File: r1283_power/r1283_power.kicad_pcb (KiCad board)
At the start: 2 copper layers, 50 x 23.5 mm, 23 parts, among them J6 Output, J7 Input, U1 R1283K

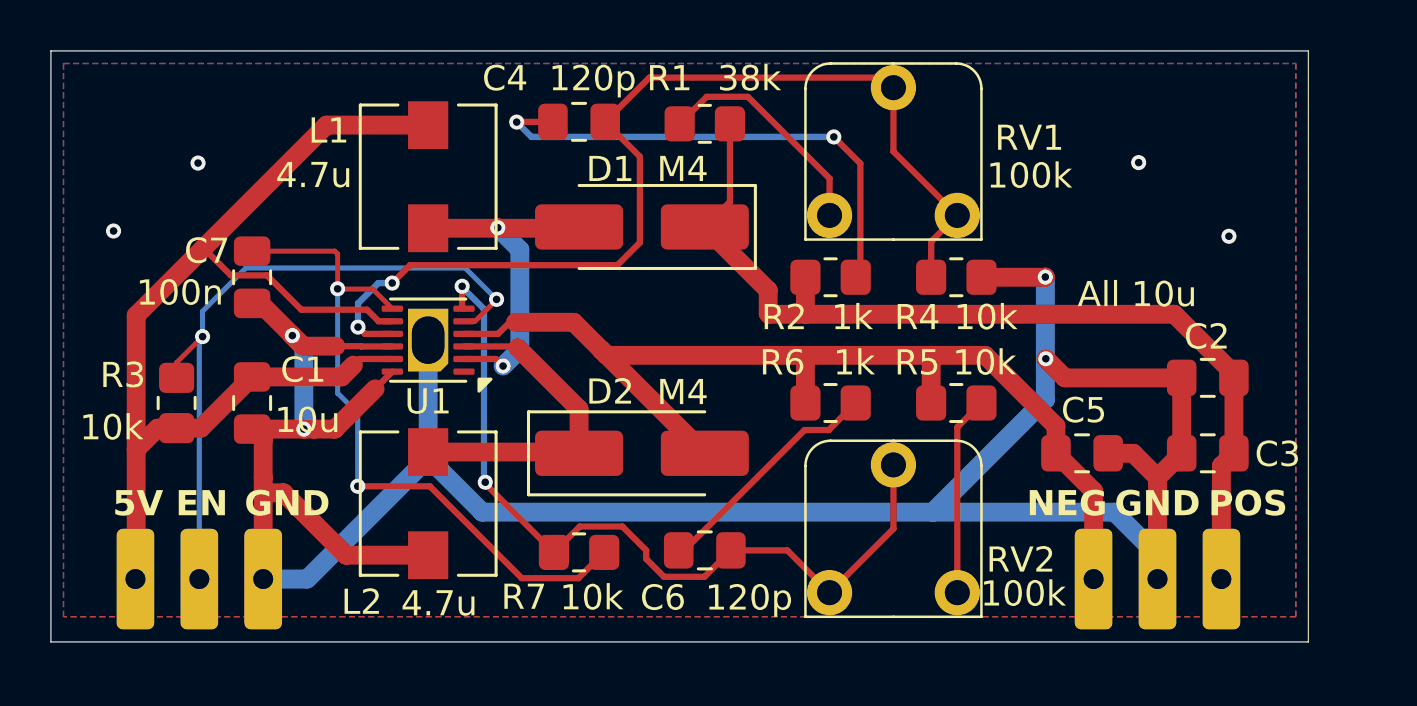
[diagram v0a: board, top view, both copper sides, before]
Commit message: added DFN breakout changed trim pot type in 33063_boost, 33063_invert, r1283_power boards fixed error in 33063_boost board (move trim pot to higher side of voltage divider)
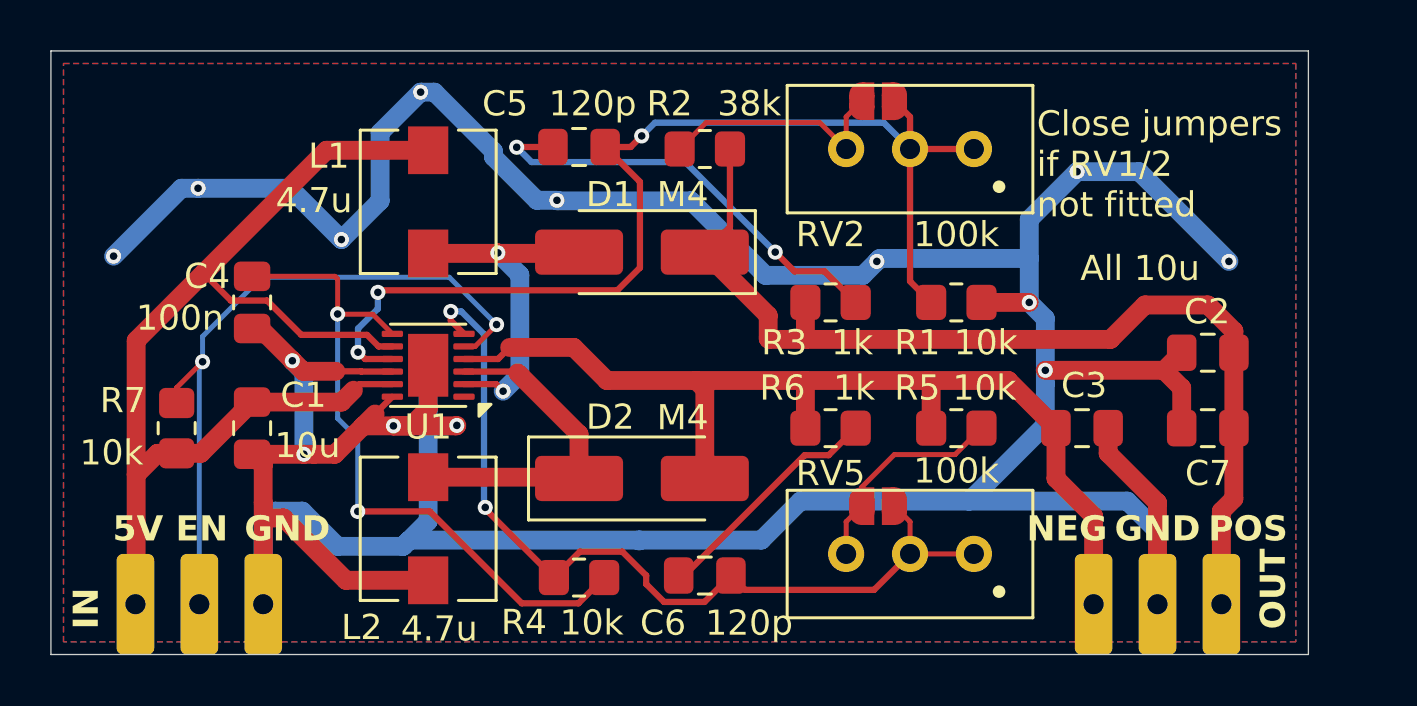
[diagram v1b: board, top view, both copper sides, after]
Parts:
- added JP1: Jumper_2_Open, Jumper:SolderJumper-2_P1.3mm_Open_RoundedPad1.0x1.5mm, F.Cu at (82.9, 52.0)
- added JP2: Jumper_2_Open, Jumper:SolderJumper-2_P1.3mm_Open_RoundedPad1.0x1.5mm, F.Cu at (82.9, 68.1)
- RV2: renamed from RV1; footprint misc:trim_pot -> Potentiometer_THT:Potentiometer_Bourns_3296W_Vertical
- RV5: renamed from RV2; footprint misc:trim_pot -> Potentiometer_THT:Potentiometer_Bourns_3296W_Vertical
- U1: footprint misc:DFN-12-1EP_3x3mm_P0.5mm_EP1.6x2.5mm_hole -> Package_DFN_QFN:DFN-12-1EP_3x3mm_P0.5mm_EP1.6x2.5mm
- moved RV5 3.35 mm to (86.7, 70.0)
- moved RV2 3.20 mm to (86.7, 53.9)
- moved C1 1.00 mm to (58.0, 65.0)
- moved C2 1.00 mm to (96.0, 62.0)
- moved C3 1.00 mm to (91.0, 65.0)
- moved C4 1.00 mm to (58.0, 60.0)
- moved C5 1.00 mm to (71.0, 53.8)
- moved C6 1.00 mm to (76.0, 70.9)
- moved C7 1.00 mm to (96.0, 65.0)
- moved D1 1.00 mm to (73.5, 58.0)
- moved D2 1.00 mm to (73.5, 67.0)
- moved J1 1.00 mm to (55.9, 74.0)
- moved J2 1.00 mm to (94.0, 74.0)
- moved L1 1.00 mm to (65.0, 56.0)
- moved L2 1.00 mm to (65.0, 69.0)
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- renumbered C5 to C3, C7 to C4, C4 to C5, C3 to C7, J7 to J1, J6 to J2, R4 to R1, R1 to R2, R2 to R3, R7 to R4, R3 to R7
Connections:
- C5 pad 2: Net-(U1-Vfb1) -> Net-(JP1-A)
- R1 pad 1: Net-(U1-Vfb1) -> Net-(JP1-A)
- R2 pad 2: Net-(R1-Pad2) -> Net-(JP1-B)
- RV2 pad 1: Net-(R1-Pad2) -> Net-(JP1-A)
- RV2 pad 2: Net-(U1-Vfb1) -> Net-(JP1-A)
- RV2 pad 3: Net-(U1-Vfb1) -> Net-(JP1-B)
- U1 pad 9: Net-(U1-Vfb1) -> Net-(JP1-A)
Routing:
- net GND1: track 105.4 -> 175.4 mm, vias 8 -> 14
- net Net-(JP1-A): track 0.00 -> 44.5 mm, vias 0 -> 3
- net Net-(U1-Vfb1): track 41.4 -> 0.00 mm, vias 2 -> 0
- net Net-(JP1-B): track 0.00 -> 9.65 mm
- net Net-(R1-Pad2): track 9.22 -> 0.00 mm
- net Net-(C5-Pad1): track 20.4 -> 17.5 mm
- net Net-(JP2-A): track 32.7 -> 35.4 mm
- net /VOUT_POS: track 38.4 -> 41.1 mm
- net /VOUT_NEG: track 41.6 -> 40.6 mm
- net Net-(JP2-B): track 7.94 -> 8.64 mm
- net /ENABLE: track 27.3 -> 27.8 mm
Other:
- board size 50 x 23.5 mm -> 50 x 24 mm
- board text added: "Close jumpers if RV1/2 not fitted"
- board text added: "IN"
- board text added: "OUT"
- board text added: "VOUT_POS = (R1 + RV1 + R2) / R2 VOUT_NEG = -1.2 * (R5 + RV5) / R4"
